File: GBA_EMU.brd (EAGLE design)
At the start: 130.7 x 72.9 mm, 82 parts, among them J1 USB-MINIB-5PIN, J2 AVR_SPI, Q1 MOSFET-PCHANNEL, SW1 LEFT, SW2 RIGHT, SW3 PWR_SWITCH, U2 FT230X, U4 LM4875, U5 V_REG_LDOSMD2, U7 AZV321, X2 HEADPHONE

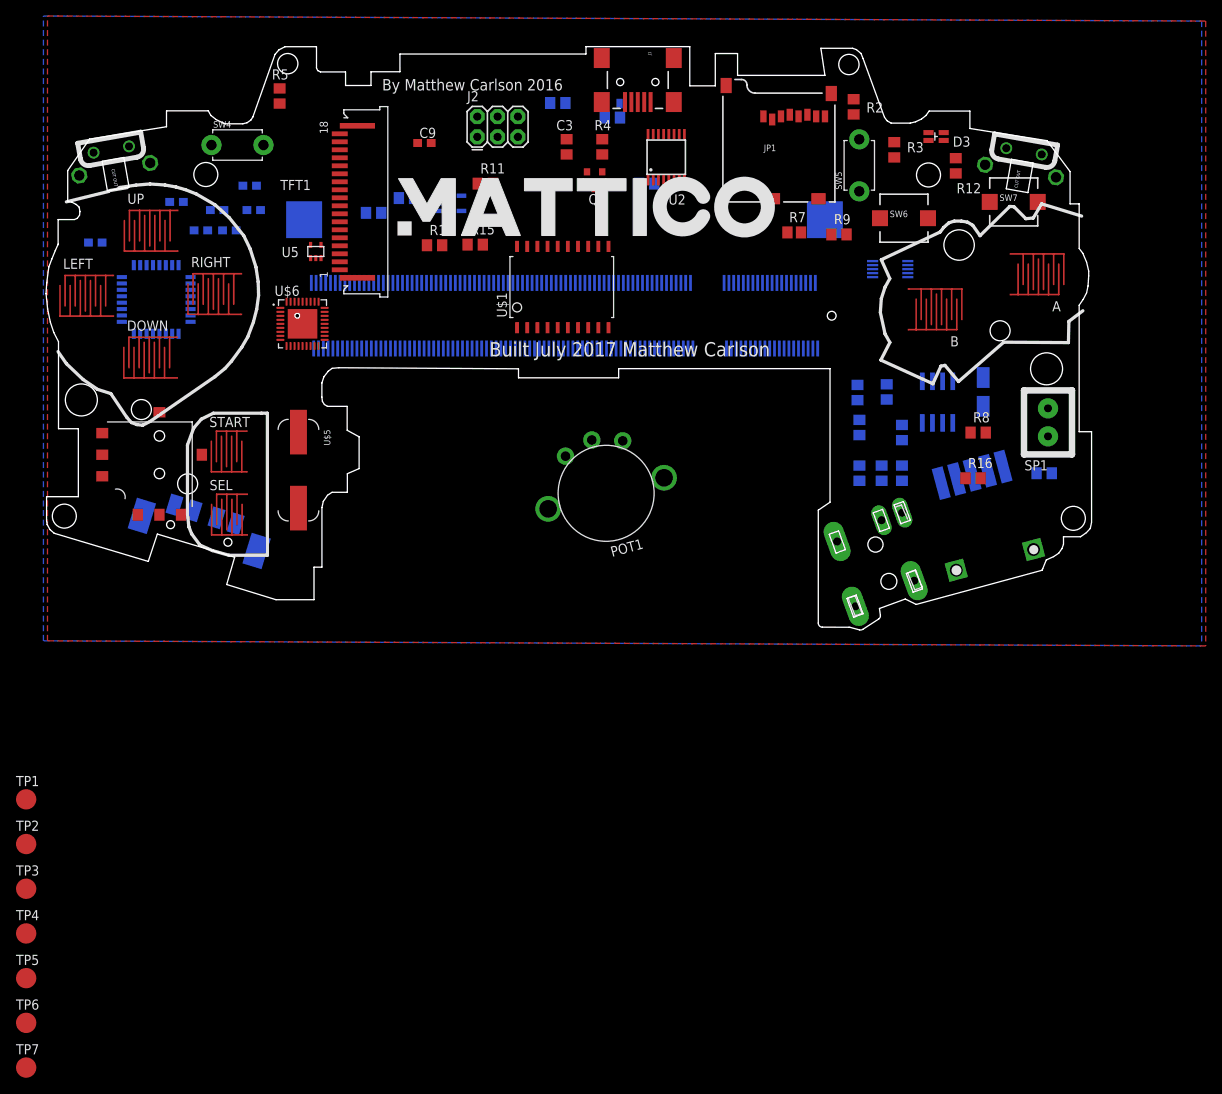
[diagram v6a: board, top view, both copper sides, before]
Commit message: added the battery charging circuit
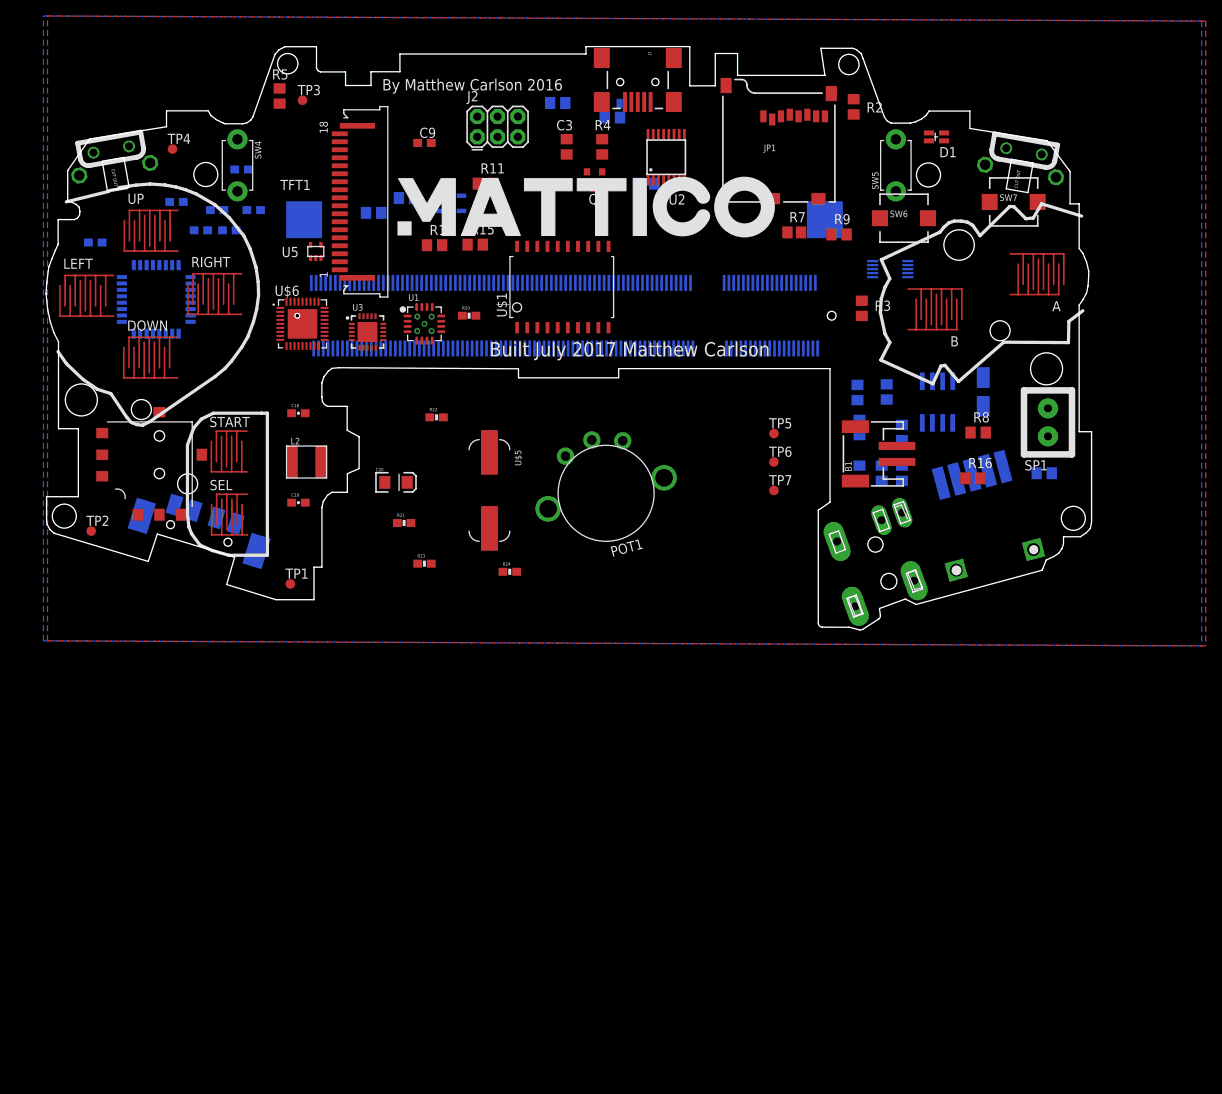
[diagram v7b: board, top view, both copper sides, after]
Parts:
- removed D3: DUAL_LED, GBA:DUAL_LED
- removed R12: 620R, rcl:R0805
- added B1: (no value), custom:MICROBUILDER_JSTPH2
- added C16: 1.0uF, SparkFun-Capacitors:0603-CAP
- added C19: 0.1uF, SparkFun-Capacitors:0603-CAP
- added C20: 100uF, SparkFun-Capacitors:EIA3216
- added D1: DUAL_LED, custom:DUAL_LED
- added L2: (no value), custom:MICROBUILDER_INDUCTOR_4.9X4.9MM
- added R20: 200k, SparkFun-Resistors:0603-RES
- added R21: 270k, SparkFun-Resistors:0603-RES
- added R22: 100k, SparkFun-Resistors:0603-RES
- added R23, R24: 1K, SparkFun-Resistors:0603-RES
- added U1: (no value), custom:MICROBUILDER_PVQFN-16
- added U3: (no value), custom:MICROBUILDER_QFN20_4MM
- TP1, TP2, TP3, TP4, TP5, TP6, TP7: value TPB2,54 -> PTR1TP12R; device testpad:B2,54 -> testpad:TP12R
- U5: value V_REG_LDOSMD2 -> Mic5365-2.8Y
- moved TP7 118.1 mm to (112.3, 26.4)
- moved TP6 116.8 mm to (112.3, 30.0)
- moved TP5 115.6 mm to (112.3, 33.5)
- moved TP3 104.4 mm to (53.3, 75.2)
- moved TP4 99.7 mm to (37.1, 69.1)
- moved TP1 42.6 mm to (51.8, 14.7)
- moved TP2 40.0 mm to (26.9, 21.3)
- moved U$5 24.0 mm to (76.7, 26.4)
- moved R3 20.2 mm to (123.2, 49.2)
- moved SW5 4.57 mm to (127.5, 67.1)
- moved SW4 2.54 mm to (45.2, 67.1), turned to 270 degrees
- moved R13 2.27 mm to (45.7, 66.5)
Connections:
- new net N$30: L2.P$2, U1.3, U1.4
- new net N$31: R20.1, U1.11
- new net N$32: R21.1, R22.2, U3.P$2
- new net N$33: R24.1, U3.P$7
- new net N$34: R23.1, U3.P$8
- new net N$35: B1.2, U3.P$14, U3.P$15, U3.P$16
- new net N$36: R23.2
- new net N$37: D1.3, R24.2
- new net N$38: R18.1
- new net PGND: U1.5, U1.6, U1.7, U1.P$18, U1.P$19, U1.P$20, U1.P$21, U1.P$22
- new net V_BATT: C16.1, C19.1, L2.P$1, R20.2, U1.8
- new net V_USB: D1.4, R21.2, U3.P$18, U3.P$19
- net 2.8V: now also TP3.TP
- net 3.3V: now also TP2.TP
- net 5V: now also C20.A, TP1.TP, U1.1, U1.15, U1.16
- net A_BTN: now also COPRO.10
- net B_BTN: now also COPRO.11
- net GND: now also B1.1, C16.2, C19.2, C20.C, R22.1, TP4.TP, U1.10, U1.13; no longer R12.2
- net N$23: now also R17.1; no longer D3.2, R12.1
- net SELECT: now also COPRO.13
- net START: now also COPRO.12
- net Z_BTN: now also COPRO.14

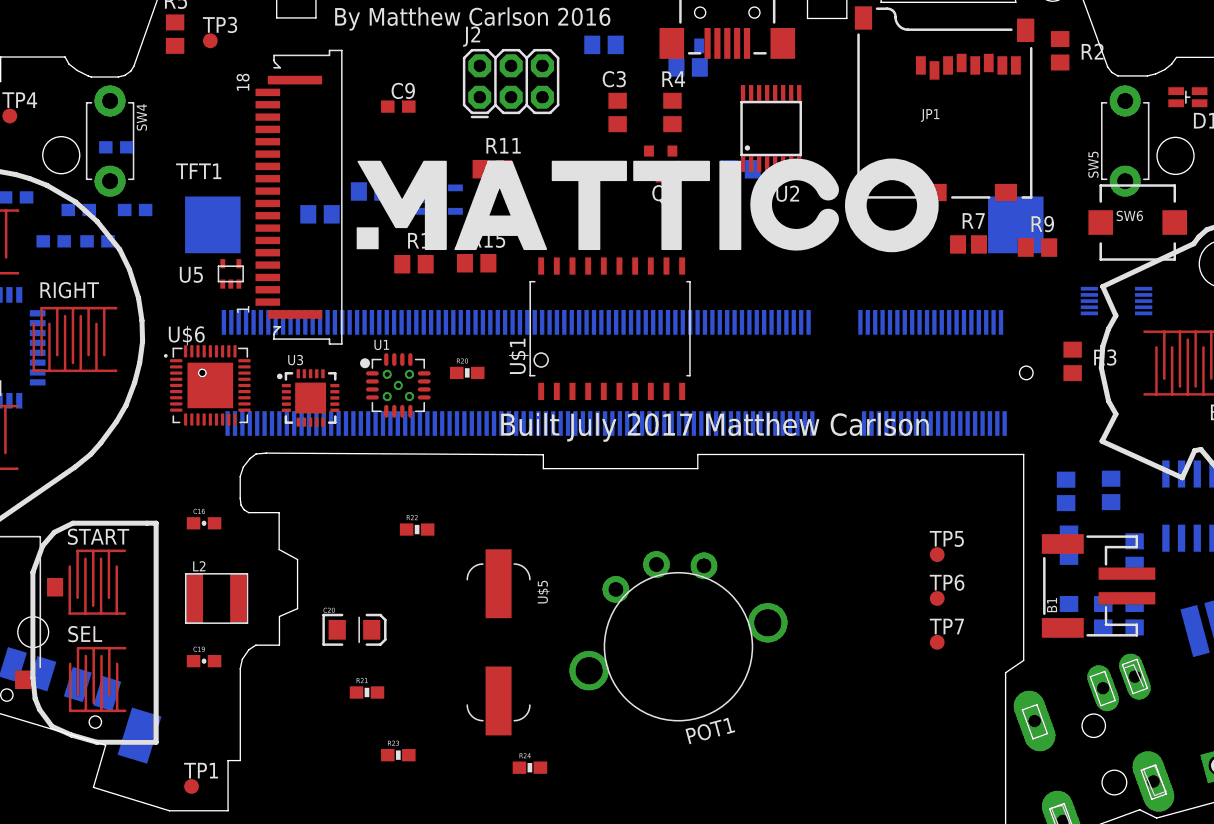
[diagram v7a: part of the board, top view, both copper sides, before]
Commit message: added a fan for overheating?
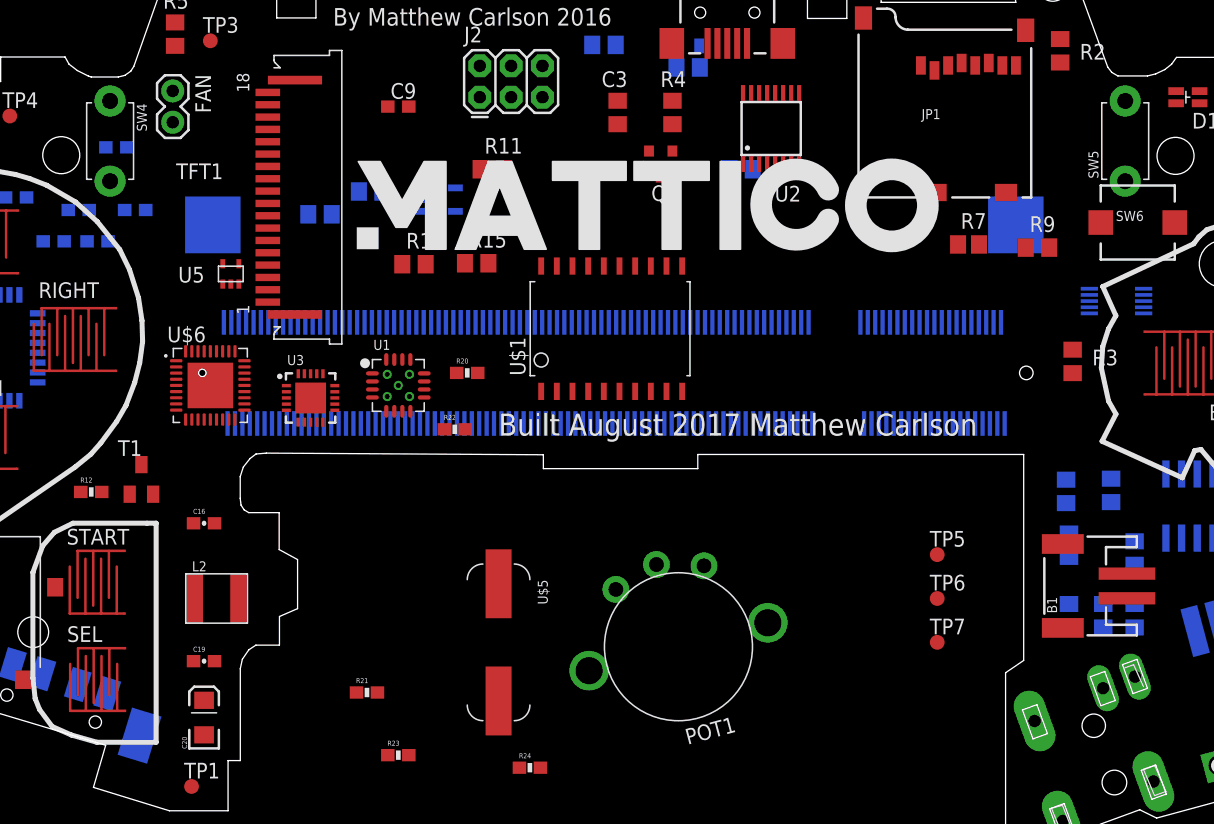
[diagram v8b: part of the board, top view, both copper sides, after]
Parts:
- added FAN: (no value), SparkFun-Connectors:1X02
- added R12: 1K, SparkFun-Resistors:0603-RES
- added T1: (no value), custom:TRANSISTOR_SC59-BEC
- moved C20 14.1 mm to (52.8, 20.3), turned to 90 degrees
- moved R22 8.68 mm to (73.2, 43.7)
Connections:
- new net FAN_EN: R12.2
- new net N$39: FAN.1, T1.C
- new net N$40: R12.1, T1.B
- net 5V: now also FAN.2
- net GND: now also T1.E
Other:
- board text added: "Built August 2017 Matthew Carlson"
- board text removed: "Built July 2017 Matthew Carlson"
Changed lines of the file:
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@@
 <hole x="25.69559375" y="37.732890625" drill="4"/>
 <wire x1="80.33825" y1="41.623790625" x2="57.87603125" y2="41.75745" width="0" layer="20"/>
-<text x="76.708" y="43.18" size="1.778" layer="21">Built July 2017 Matthew Carlson</text>
+<text x="76.708" y="43.18" size="1.778" layer="21">Built August 2017 Matthew Carlson</text>
 </plain>
 <attributes>
@@
 <attribute name="PROD_ID" value="CAP-00810" x="52.832" y="24.892" size="1.778" layer="27" display="off"/>
 </element>
-<element name="C20" library="SparkFun-Capacitors" package="EIA3216" value="100uF" x="65.024" y="27.432"/>
+<element name="C20" library="SparkFun-Capacitors" package="EIA3216" value="100uF" x="52.832" y="20.32" rot="R90"/>
 <element name="R21" library="SparkFun-Resistors" package="0603-RES" value="270k" x="66.04" y="22.352">
 <attribute name="PROD_ID" value="RES-09385" x="66.04" y="22.352" size="1.778" layer="27" display="off"/>
 </element>
-<element name="R22" library="SparkFun-Resistors" package="0603-RES" value="100k" x="70.104" y="35.56">
-<attribute name="PROD_ID" value="RES-07828" x="70.104" y="35.56" size="1.778" layer="27" display="off"/>
+<element name="R22" library="SparkFun-Resistors" package="0603-RES" value="100k" x="73.152" y="43.688">
+<attribute name="PROD_ID" value="RES-07828" x="73.152" y="43.688" size="1.778" layer="27" display="off"/>
 </element>
 <element name="R23" library="SparkFun-Resistors" package="0603-RES" value="1K" x="68.58" y="17.272">
@@
 <element name="TP7" library="testpad" package="TP12R" value="PTR1TP12R" x="112.268" y="26.416">
 <attribute name="TP_SIGNAL_NAME" value="" x="112.268" y="26.416" size="1.778" layer="27" display="off"/>
+</element>
+<element name="FAN" library="SparkFun-Connectors" package="1X02" value="" x="50.292" y="71.12" rot="R270"/>
+<element name="T1" library="custom" package="TRANSISTOR_SC59-BEC" value="" x="47.752" y="39.624"/>
+<element name="R12" library="SparkFun-Resistors" package="0603-RES" value="1K" x="43.688" y="38.608">
+<attribute name="PROD_ID" value="RES-07856" x="43.688" y="38.608" size="1.778" layer="27" display="off"/>
 </element>
 </elements>
@@
 <contactref element="B1" pad="1"/>
 <contactref element="U$1" pad="P$10"/>
+<contactref element="T1" pad="E"/>
 <wire x1="139.24" y1="62.484" x2="141.835725" y2="50.90233125" width="0" layer="19" extent="1-1"/>
+<wire x1="72.74" y1="44.16" x2="72.302" y2="43.688" width="0" layer="19" extent="1-16"/>
+<wire x1="70.94" y1="44.16" x2="72.302" y2="43.688" width="0" layer="19" extent="1-16"/>
 <wire x1="58.04" y1="52.36" x2="58" y2="54" width="0" layer="19" extent="1-16"/>
 <wire x1="115.94" y1="44.16" x2="117.74" y2="44.16" width="0" layer="19" extent="16-16"/>
@@
 <wire x1="108.74" y1="44.16" x2="110.54" y2="44.16" width="0" layer="19" extent="16-16"/>
 <wire x1="106.94" y1="44.16" x2="108.74" y2="44.16" width="0" layer="19" extent="16-16"/>
-<wire x1="59.84" y1="52.36" x2="58.04" y2="52.36" width="0" layer="19" extent="16-16"/>
-<wire x1="99.131" y1="65.197" x2="97.31125" y2="64.77" width="0" layer="19" extent="1-16"/>
-<wire x1="55.64" y1="52.36" x2="58.04" y2="52.36" width="0" layer="19" extent="16-16"/>
-<wire x1="70.68" y1="46.919" x2="69.555" y2="49.344" width="0" layer="19" extent="1-1"/>
-<wire x1="90.74" y1="44.16" x2="91.59" y2="46.764" width="0" layer="19" extent="1-16"/>
+<wire x1="74.54" y1="44.16" x2="72.74" y2="44.16" width="0" layer="19" extent="16-16"/>
+<wire x1="76.34" y1="44.16" x2="74.54" y2="44.16" width="0" layer="19" extent="16-16"/>
+<wire x1="78.14" y1="44.16" x2="76.34" y2="44.16" width="0" layer="19" extent="16-16"/>
+<wire x1="79.94" y1="44.16" x2="78.14" y2="44.16" width="0" layer="19" extent="16-16"/>
+<wire x1="81.74" y1="44.16" x2="79.94" y2="44.16" width="0" layer="19" extent="16-16"/>
+<wire x1="83.54" y1="44.16" x2="81.74" y2="44.16" width="0" layer="19" extent="16-16"/>
+<wire x1="85.34" y1="44.16" x2="83.54" y2="44.16" width="0" layer="19" extent="16-16"/>
+<wire x1="87.14" y1="44.16" x2="85.34" y2="44.16" width="0" layer="19" extent="16-16"/>
+<wire x1="88.94" y1="44.16" x2="87.14" y2="44.16" width="0" layer="19" extent="16-16"/>
+<wire x1="90.74" y1="44.16" x2="88.94" y2="44.16" width="0" layer="19" extent="16-16"/>
 <wire x1="92.54" y1="44.16" x2="90.74" y2="44.16" width="0" layer="19" extent="16-16"/>
 <wire x1="94.34" y1="44.16" x2="92.54" y2="44.16" width="0" layer="19" extent="16-16"/>
@@
 <wire x1="99.74" y1="44.16" x2="97.94" y2="44.16" width="0" layer="19" extent="16-16"/>
 <wire x1="101.54" y1="44.16" x2="99.74" y2="44.16" width="0" layer="19" extent="16-16"/>
-<wire x1="88.94" y1="44.16" x2="90.74" y2="44.16" width="0" layer="19" extent="16-16"/>
-<wire x1="87.14" y1="44.16" x2="88.94" y2="44.16" width="0" layer="19" extent="16-16"/>
-<wire x1="85.34" y1="44.16" x2="87.14" y2="44.16" width="0" layer="19" extent="16-16"/>
-<wire x1="83.54" y1="44.16" x2="85.34" y2="44.16" width="0" layer="19" extent="16-16"/>
-<wire x1="81.74" y1="44.16" x2="83.54" y2="44.16" width="0" layer="19" extent="16-16"/>
-<wire x1="79.94" y1="44.16" x2="81.74" y2="44.16" width="0" layer="19" extent="16-16"/>
-<wire x1="78.14" y1="44.16" x2="79.94" y2="44.16" width="0" layer="19" extent="16-16"/>
-<wire x1="76.34" y1="44.16" x2="78.14" y2="44.16" width="0" layer="19" extent="16-16"/>
-<wire x1="74.54" y1="44.16" x2="76.34" y2="44.16" width="0" layer="19" extent="16-16"/>
-<wire x1="72.74" y1="44.16" x2="74.54" y2="44.16" width="0" layer="19" extent="16-16"/>
-<wire x1="70.94" y1="44.16" x2="72.74" y2="44.16" width="0" layer="19" extent="16-16"/>
 <wire x1="69.14" y1="44.16" x2="70.94" y2="44.16" width="0" layer="19" extent="16-16"/>
+<wire x1="59.84" y1="52.36" x2="58.04" y2="52.36" width="0" layer="19" extent="16-16"/>
 <wire x1="67.34" y1="44.16" x2="69.14" y2="44.16" width="0" layer="19" extent="16-16"/>
 <wire x1="65.54" y1="44.16" x2="67.34" y2="44.16" width="0" layer="19" extent="16-16"/>
 <wire x1="63.74" y1="44.16" x2="65.54" y2="44.16" width="0" layer="19" extent="16-16"/>
+<wire x1="99.131" y1="65.197" x2="97.31125" y2="64.77" width="0" layer="19" extent="1-16"/>
+<wire x1="55.64" y1="52.36" x2="58.04" y2="52.36" width="0" layer="19" extent="16-16"/>
+<wire x1="70.68" y1="46.919" x2="69.555" y2="49.344" width="0" layer="19" extent="1-1"/>
 <wire x1="68.84" y1="52.36" x2="69.555" y2="49.344" width="0" layer="19" extent="1-16"/>
 <wire x1="70.64" y1="52.36" x2="68.84" y2="52.36" width="0" layer="19" extent="16-16"/>
@@
 <wire x1="53.34" y1="47.244" x2="55.94" y2="44.16" width="0" layer="19" extent="1-16"/>
 <wire x1="29.69269375" y1="53.293165625" x2="34.652" y2="54.5846" width="0" layer="19" extent="1-16"/>
+<wire x1="46.387653125" y1="33.8340125" x2="48.702" y2="38.424" width="0" layer="19" extent="1-1"/>
 <wire x1="106.64" y1="52.36" x2="101.24" y2="52.36" width="0" layer="19" extent="16-16"/>
 <wire x1="108.44" y1="52.36" x2="106.64" y2="52.36" width="0" layer="19" extent="16-16"/>
@@
 <wire x1="129.090321875" y1="46.519734375" x2="132.08" y2="40.065" width="0" layer="19" extent="1-16"/>
 <wire x1="46.42191875" y1="25.943271875" x2="53.682" y2="24.892" width="0" layer="19" extent="1-1"/>
-<wire x1="46.387653125" y1="33.8340125" x2="53.682" y2="36.068" width="0" layer="19" extent="1-1"/>
-<wire x1="69.254" y1="35.56" x2="69.14" y2="44.16" width="0" layer="19" extent="1-16"/>
 </signal>
 <signal name="TXD">
@@
 <contactref element="U1" pad="1"/>
 <contactref element="C20" pad="A"/>
+<contactref element="FAN" pad="2"/>
 <wire x1="134.62" y1="34.865" x2="140.905878125" y2="29.401509375" width="0" layer="19" extent="16-16"/>
 <wire x1="128.27" y1="32.705" x2="134.62" y2="34.865" width="0" layer="19" extent="16-16"/>
@@
 <wire x1="55.65" y1="55.46125" x2="66.48" y2="48.219" width="0" layer="19" extent="1-1"/>
 <wire x1="54.35" y1="55.46125" x2="55.65" y2="55.46125" width="0" layer="19" extent="1-1"/>
+<wire x1="50.292" y1="68.58" x2="54.35" y2="55.46125" width="0" layer="19" extent="1-1"/>
 <wire x1="39.3446" y1="50.692" x2="54.35" y2="55.46125" width="0" layer="19" extent="1-16"/>
 <wire x1="37.852" y1="54.5846" x2="39.3446" y2="50.692" width="0" layer="19" extent="16-16"/>
 <wire x1="37.052" y1="54.5846" x2="37.852" y2="54.5846" width="0" layer="19" extent="16-16"/>
 <wire x1="28.282" y1="57.404" x2="37.052" y2="54.5846" width="0" layer="19" extent="16-16"/>
-<wire x1="66.424" y1="27.432" x2="66.48" y2="48.219" width="0" layer="19" extent="1-1"/>
-<wire x1="51.816" y1="14.732" x2="66.424" y2="27.432" width="0" layer="19" extent="1-1"/>
+<wire x1="52.832" y1="21.72" x2="66.48" y2="48.219" width="0" layer="19" extent="1-1"/>
+<wire x1="51.816" y1="14.732" x2="52.832" y2="21.72" width="0" layer="19" extent="1-1"/>
 </signal>
 <signal name="PWM0">
@@
 <contactref element="R22" pad="2"/>
 <contactref element="U3" pad="P$2"/>
-<wire x1="65.19" y1="22.352" x2="70.954" y2="35.56" width="0" layer="19" extent="1-1"/>
-<wire x1="59.503" y1="46.728" x2="70.954" y2="35.56" width="0" layer="19" extent="1-1"/>
+<wire x1="59.503" y1="46.728" x2="74.002" y2="43.688" width="0" layer="19" extent="1-1"/>
+<wire x1="65.19" y1="22.352" x2="74.002" y2="43.688" width="0" layer="19" extent="1-1"/>
 </signal>
 <signal name="N$33">
@@
 <contactref element="R18" pad="1"/>
 </signal>
+<signal name="N$39">
+<contactref element="FAN" pad="1"/>
+<contactref element="T1" pad="C"/>
+<wire x1="47.752" y1="40.824" x2="50.292" y2="71.12" width="0" layer="19" extent="1-1"/>
+</signal>
+<signal name="N$40">
+<contactref element="T1" pad="B"/>
+<contactref element="R12" pad="1"/>
+<wire x1="42.838" y1="38.608" x2="46.802" y2="38.424" width="0" layer="19" extent="1-1"/>
+</signal>
+<signal name="FAN_EN">
+<contactref element="R12" pad="2"/>
+</signal>
 </signals>
